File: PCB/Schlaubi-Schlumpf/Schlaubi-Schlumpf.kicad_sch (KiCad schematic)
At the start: 2 parts, among them J6 TYPE-C-31-M-12

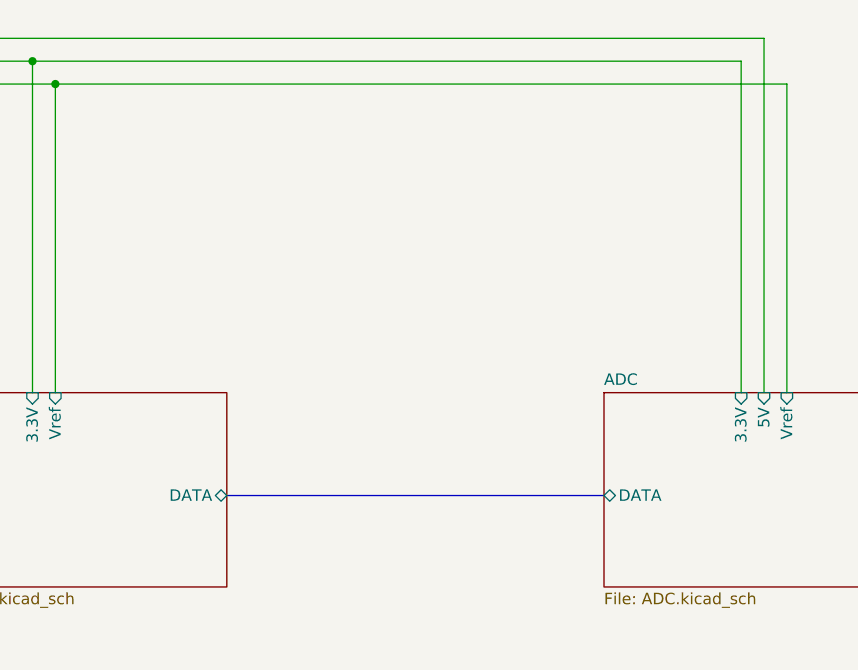
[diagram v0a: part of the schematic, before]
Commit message: added IMU
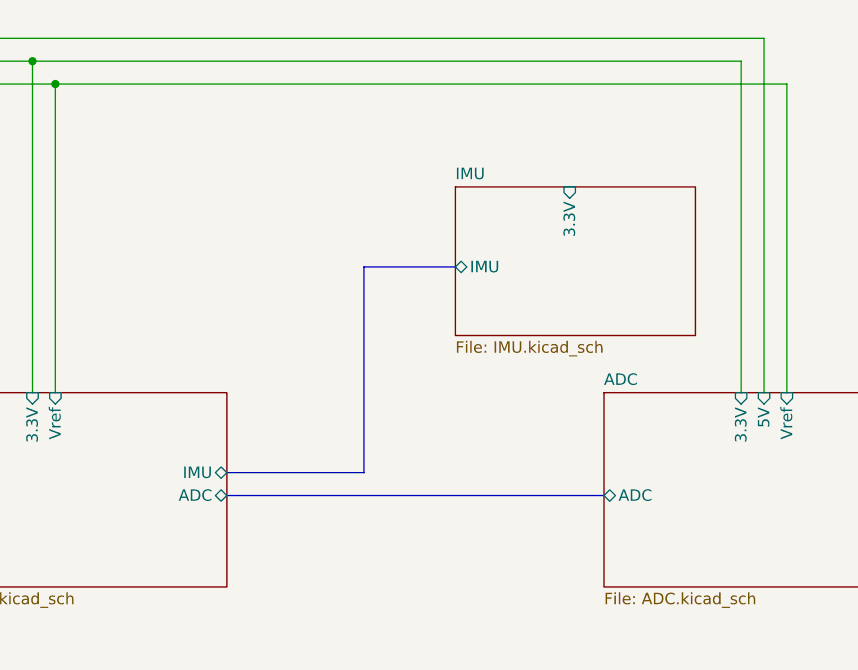
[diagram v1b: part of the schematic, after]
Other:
- added sheet IMU (IMU.kicad_sch)
- sheet ADC ports: added ADC; removed DATA
- sheet ESP32 ports: added ADC, IMU; removed DATA
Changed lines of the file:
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@@
+		)
+	)
+	(bus
+		(pts
+			(xy 203.2 55.88) (xy 193.04 55.88)
+		)
+		(stroke
+			(width 0)
+			(type default)
+		)
+	)
+	(bus
+		(pts
+			(xy 193.04 55.88) (xy 193.04 78.74)
+		)
+		(stroke
+			(width 0)
+			(type default)
+		)
+	)
+	(bus
+		(pts
+			(xy 193.04 78.74) (xy 177.8 78.74)
+		)
+		(stroke
+			(width 0)
+			(type default)
 		)
 	)
@@
 		)
 	)
+	(bus
+		(pts
+			(xy 177.8 81.28) (xy 219.71 81.28)
+		)
+		(stroke
+			(width 0)
+			(type default)
+		)
+	)
 	(wire
 		(pts
 			(xy 156.21 33.02) (xy 156.21 69.85)
-		)
-		(stroke
-			(width 0)
-			(type default)
-		)
-	)
-	(bus
-		(pts
-			(xy 177.8 81.28) (xy 219.71 81.28)
 		)
 		(stroke
@@
 			)
 		)
-		(pin "DATA" bidirectional
+		(pin "ADC" bidirectional
 			(at 219.71 81.28 180)
 			(effects
@@
 			)
 		)
-		(pin "DATA" bidirectional
+		(pin "IMU" bidirectional
+			(at 177.8 78.74 0)
+			(effects
+				(font
+					(size 1.27 1.27)
+				)
+				(justify right)
+			)
+		)
+		(pin "ADC" bidirectional
 			(at 177.8 81.28 0)
 			(effects
@@
 				)
 			)
+		)
+	)
+	(sheet
+		(at 203.2 46.99)
+		(size 26.67 16.51)
+		(fields_autoplaced yes)
+		(stroke
+			(width 0.1524)
+			(type solid)
+		)
+		(fill
+			(color 0 0 0 0.0000)
+		)
+		(property "Sheetname" "IMU"
+			(at 203.2 46.2784 0)
+			(effects
+				(font
+					(size 1.27 1.27)
+				)
+				(justify left bottom)
+			)
+		)
+		(property "Sheetfile" "IMU.kicad_sch"
+			(at 203.2 64.0846 0)
+			(effects
+				(font
+					(size 1.27 1.27)
+				)
+				(justify left top)
+			)
+		)
+		(pin "3.3V" input
+			(at 215.9 46.99 90)
+			(effects
+				(font
+					(size 1.27 1.27)
+				)
+				(justify right)
+			)
+		)
+		(pin "IMU" bidirectional
+			(at 203.2 55.88 180)
+			(effects
+				(font
+					(size 1.27 1.27)
+				)
+				(justify left)
+			)
+		)
+		(instances
+			(project "Schlaubi-Schlumpf"
+				(path "/adec948c-82e6-4ad4-8e75-b19e612c0d17"
+					(page "10")
+				)
+			)

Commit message: v1
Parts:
- added D8: TPD4E05U06DQAR, TPD4E05U06DQAR:DQA_R-PUSON-N10_, symbol TPD4E05U06DQAR:TPD4E05U06DQAR
- added H1, H2, H3: MountingHole_Pad, MountingHole:MountingHole_3.2mm_M3_Pad, symbol Mechanical:MountingHole_Pad
- added J7: RFShield_TwoPieces, RF_Shielding:Laird_Technologies_BMI-S-204-F_32.00x32.00mm, symbol Device:RFShield_TwoPieces
- added JP_SH/USB1: SolderJumper_2_Bridged, Jumper:SolderJumper-2_P1.3mm_Bridged2Bar_RoundedPad1.0x1.5mm, symbol Jumper:SolderJumper_2_Bridged
- added R19, R20: 5.1k, Resistor_SMD:R_0603_1608Metric, symbol Device:R
- JP_SH/GND1: renamed from JP_SH/GND; footprint (none) -> Jumper:SolderJumper-2_P1.3mm_Bridged2Bar_RoundedPad1.0x1.5mm
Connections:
- net D+: now also D8.1 (D1+), D8.10 (NC_4)
- net D-: now also D8.2 (D1-), D8.9 (NC_3)
- net GND: now also D8.3 (GND_1), D8.8 (GND_2), R19.1, R20.1
- net Shield: now also H1.1, H2.1, H3.1, J7.1 (Shield), JP_SH/USB1.2 (B); no longer J6.S1 (SHIELD), J6.S2 (SHIELD), J6.S3 (SHIELD), J6.S4 (SHIELD)
- net CC: no longer names the net of J6.A5 (CC1)
- net CC: now also R19.2; no longer J6.B5 (CC2)
- net Power_battery/Vbus renamed Vbus
- net Vbus: now also D8.4 (D2+), D8.7 (NC_2)
- net SBU: no longer names the net of J6.A8 (SBU1)
- net SBU: no longer J6.B8 (SBU2)
- new net: J6.B5 (CC2), R20.2
- new net: J6.S1 (SHIELD), J6.S2 (SHIELD), J6.S3 (SHIELD), J6.S4 (SHIELD), JP_SH/USB1.1 (A)
- no-connect marks 0 -> 4
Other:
- sheet ADC ports: added ADC{MISO SCLK *CS MOSI *DRDY START *RESET}; removed ADC
- sheet ESP32 ports: added ADC{MISO SCLK *CS MOSI *DRDY START *RESET}, IMU{SCL/SCLK,SDA/MOSI,SDO/MISO,CS,Interrupt}; removed ADC, IMU
- sheet IMU ports: added IMU{SCL/SCLK,SDA/MOSI,SDO/MISO,CS,Interrupt}; removed IMU
- note added: "Abstandshalter? SMTSOM325BTR"
- note added: "ESD-Protection"
- moved on the sheet: J6

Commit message: updates
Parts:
- removed H1, H3: MountingHole_Pad, MountingHole:MountingHole_3.2mm_M3_Pad, symbol Mechanical:MountingHole_Pad
- H2: now in the parts list
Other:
- moved on the sheet: H2
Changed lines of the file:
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@@
-	)
-	(junction
-		(at 25.4 128.27)
-		(diameter 0)
-		(color 0 0 0 0)
 	)
 	(junction
@@
 	)
 	(junction
-		(at 25.4 123.19)
-		(diameter 0)
-		(color 0 0 0 0)
-	)
-	(junction
 		(at 69.85 26.67)
 		(diameter 0)
@@
 	(wire
 		(pts
-			(xy 25.4 123.19) (xy 25.4 128.27)
-		)
-		(stroke
-			(width 0)
-			(type default)
-		)
-	)
-	(wire
-		(pts
 			(xy 71.12 26.67) (xy 69.85 26.67)
 		)
@@
 		(pts
 			(xy 215.9 33.02) (xy 215.9 46.99)
-		)
-		(stroke
-			(width 0)
-			(type default)
-		)
-	)
-	(wire
-		(pts
-			(xy 25.4 128.27) (xy 25.4 133.35)
 		)
 		(stroke
@@
 		(at 22.86 123.19 90)
 		(unit 1)
-		(exclude_from_sim yes)
-		(in_bom no)
+		(exclude_from_sim no)
+		(in_bom yes)
 		(on_board yes)
 		(dnp no)
 		(fields_autoplaced yes)
-		(property "Reference" "H1"
+		(property "Reference" "H2"
 			(at 21.59 116.84 90)
 			(effects
@@
 		(property "Description" "Mounting Hole with connection"
 			(at 22.86 123.19 0)
-			(effects
-				(font
-					(size 1.27 1.27)
-				)
-				(hide yes)
-			)
-		)
-		(pin "1"
-		)
-		(instances
-			(project ""
-				(path "/adec948c-82e6-4ad4-8e75-b19e612c0d17"
-					(reference "H1")
-					(unit 1)
-				)
-			)
-		)
-	)
-	(symbol
-		(lib_id "Mechanical:MountingHole_Pad")
-		(at 22.86 128.27 90)
-		(unit 1)
-		(exclude_from_sim yes)
-		(in_bom no)
-		(on_board yes)
-		(dnp no)
-		(fields_autoplaced yes)
-		(property "Reference" "H2"
-			(at 21.59 121.92 90)
-			(effects
-				(font
-					(size 1.27 1.27)
-				)
-			)
-		)
-		(property "Value" "MountingHole_Pad"
-			(at 21.59 124.46 90)
-			(effects
-				(font
-					(size 1.27 1.27)
-				)
-			)
-		)
-		(property "Footprint" "MountingHole:MountingHole_3.2mm_M3_Pad"
-			(at 22.86 128.27 0)
-			(effects
-				(font
-					(size 1.27 1.27)
-				)
-				(hide yes)
-			)
-		)
-		(property "Datasheet" "~"
-			(at 22.86 128.27 0)
-			(effects
-				(font
-					(size 1.27 1.27)
-				)
-				(hide yes)
-			)
-		)
-		(property "Description" "Mounting Hole with connection"
-			(at 22.86 128.27 0)
 			(effects
 				(font
@@
 					(unit 1)
 				)
-			)
-		)
-	)
-	(symbol
-		(lib_id "Mechanical:MountingHole_Pad")
-		(at 22.86 133.35 90)
-		(unit 1)
-		(exclude_from_sim yes)
-		(in_bom no)
-		(on_board yes)
-		(dnp no)
-		(fields_autoplaced yes)
-		(property "Reference" "H3"
-			(at 21.59 127 90)
-			(effects
-				(font
-					(size 1.27 1.27)
-				)
-			)
-		)
-		(property "Value" "MountingHole_Pad"
-			(at 21.59 129.54 90)
-			(effects
-				(font
-					(size 1.27 1.27)
-				)
-			)
-		)
-		(property "Footprint" "MountingHole:MountingHole_3.2mm_M3_Pad"
-			(at 22.86 133.35 0)
-			(effects
-				(font
-					(size 1.27 1.27)
-				)
-				(hide yes)
-			)
-		)
-		(property "Datasheet" "~"
-			(at 22.86 133.35 0)
-			(effects
-				(font
-					(size 1.27 1.27)
-				)
-				(hide yes)
-			)
-		)
-		(property "Description" "Mounting Hole with connection"
-			(at 22.86 133.35 0)
-			(effects
-				(font
-					(size 1.27 1.27)
-				)
-				(hide yes)
-			)
-		)
-		(pin "1"
-		)
-		(instances
-			(project "Schlaubi-Schlumpf"
-				(path "/adec948c-82e6-4ad4-8e75-b19e612c0d17"
-					(reference "H3")
-					(unit 1)
-				)

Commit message: update Opamp
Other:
- sheet ADC ports: added ADC{MISO SCLK *CS MOSI *DRDY START *RESET *PWDN}, non_reg; removed ADC{MISO SCLK *CS MOSI *DRDY START *RESET}, Vref
- sheet ESP32 ports: added ADC{MISO SCLK *CS MOSI *DRDY START *RESET *PWDN}; removed ADC{MISO SCLK *CS MOSI *DRDY START *RESET}
- sheet Power_battery ports: added non_reg_in; removed 2V
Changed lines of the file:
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@@
-	)
-	(junction
-		(at 158.75 35.56)
-		(diameter 0)
-		(color 0 0 0 0)
 	)
 	(junction
@@
 	(wire
 		(pts
+			(xy 240.03 27.94) (xy 240.03 69.85)
+		)
+		(stroke
+			(width 0)
+			(type default)
+		)
+	)
+	(wire
+		(pts
 			(xy 85.09 44.45) (xy 78.74 44.45)
 		)
@@
 		)
 	)
+	(wire
+		(pts
+			(xy 149.86 27.94) (xy 240.03 27.94)
+		)
+		(stroke
+			(width 0)
+			(type default)
+		)
+	)
 	(bus
 		(pts
@@
 	(wire
 		(pts
-			(xy 158.75 35.56) (xy 158.75 69.85)
-		)
-		(stroke
-			(width 0)
-			(type default)
-		)
-	)
-	(wire
-		(pts
-			(xy 149.86 35.56) (xy 158.75 35.56)
-		)
-		(stroke
-			(width 0)
-			(type default)
-		)
-	)
-	(wire
-		(pts
 			(xy 149.86 33.02) (xy 156.21 33.02)
 		)
@@
 		(pts
 			(xy 156.21 33.02) (xy 215.9 33.02)
-		)
-		(stroke
-			(width 0)
-			(type default)
-		)
-	)
-	(wire
-		(pts
-			(xy 158.75 35.56) (xy 240.03 35.56)
-		)
-		(stroke
-			(width 0)
-			(type default)
-		)
-	)
-	(wire
-		(pts
-			(xy 240.03 35.56) (xy 240.03 69.85)
 		)
 		(stroke
@@
 			)
 		)
-		(pin "Vref" input
+		(pin "ADC{MISO SCLK *CS MOSI *DRDY START *RESET *PWDN}" bidirectional
+			(at 219.71 81.28 180)
+			(effects
+				(font
+					(size 1.27 1.27)
+				)
+				(justify left)
+			)
+		)
+		(pin "non_reg" input
 			(at 240.03 69.85 90)
 			(effects
@@
 				)
 				(justify right)
-			)
-		)
-		(pin "ADC{MISO SCLK *CS MOSI *DRDY START *RESET}" bidirectional
-			(at 219.71 81.28 180)
-			(effects
-				(font
-					(size 1.27 1.27)
-				)
-				(justify left)
 			)
 		)
@@
 			)
 		)
-		(pin "ADC{MISO SCLK *CS MOSI *DRDY START *RESET}" bidirectional
+		(pin "ADC{MISO SCLK *CS MOSI *DRDY START *RESET *PWDN}" bidirectional
 			(at 177.8 81.28 0)
 			(effects
@@
 	)
 	(sheet
-		(at 118.11 27.94)
-		(size 31.75 19.05)
+		(at 118.11 24.13)
+		(size 31.75 22.86)
 		(fields_autoplaced yes)
 		(stroke
@@
 		)
 		(property "Sheetname" "Power_battery"
-			(at 118.11 27.2284 0)
+			(at 118.11 23.4184 0)
 			(effects
 				(font
@@
 			)
 		)
-		(pin "2V" output
-			(at 149.86 35.56 0)
-			(effects
-				(font
-					(size 1.27 1.27)
-				)
-				(justify right)
-			)
-		)
 		(pin "3.3V" output
 			(at 149.86 33.02 0)
 			(effects
 				(font
+					(size 1.27 1.27)
+				)
+				(justify right)
+			)
+		)
+		(pin "non_reg_in" output
+			(at 149.86 27.94 0)
+			(effects
+				(font
